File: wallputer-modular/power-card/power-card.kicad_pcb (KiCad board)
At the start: 2 copper layers, 142 parts, among them J2 Power, Q1 FQP27P06, Q2 IRLZ44N, SW1 reset, U1 TLC555CD, U12 74HC04, U16 74HC04, U17 74HC04, U18 74HC04, U2 74HC04, U3 74HC04

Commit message: fix drc
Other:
- board outline added: 100.3 x 99.7 mm

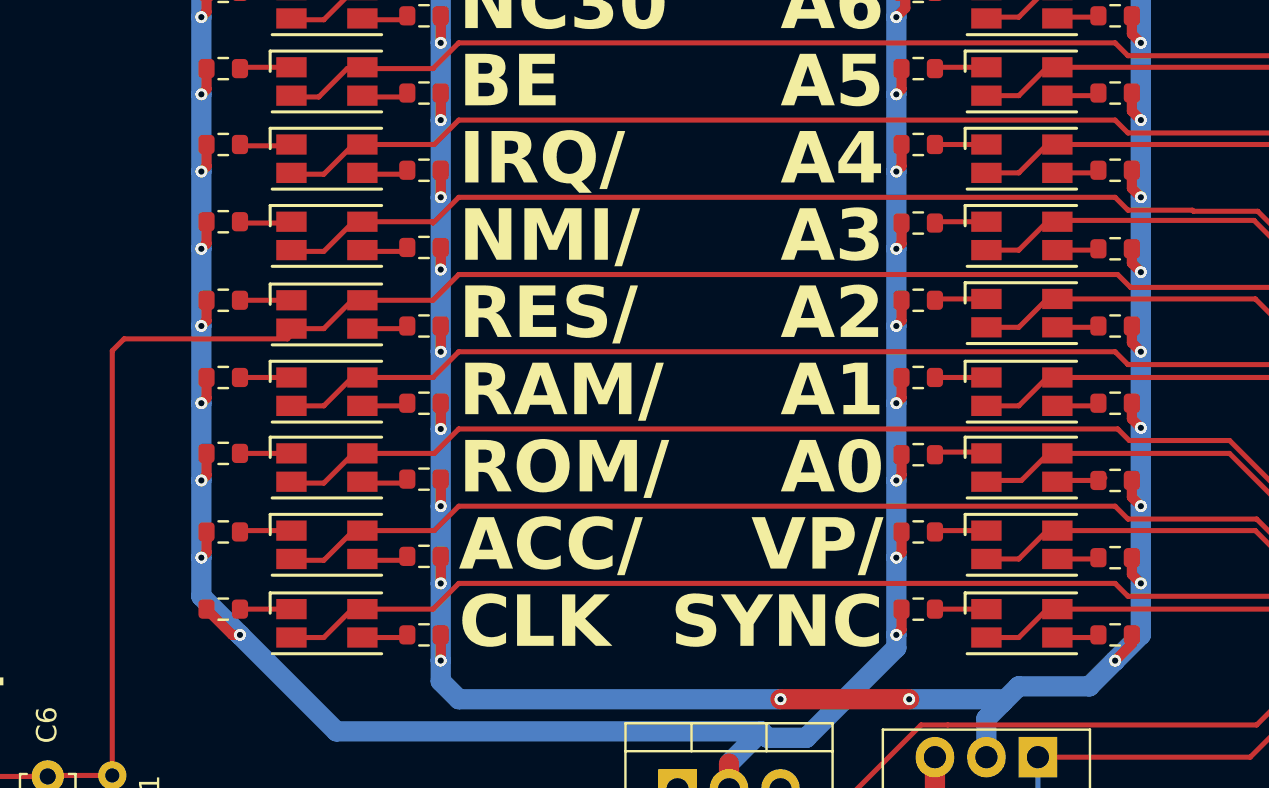
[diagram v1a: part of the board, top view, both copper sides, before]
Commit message: replace dual leds with single for some signals
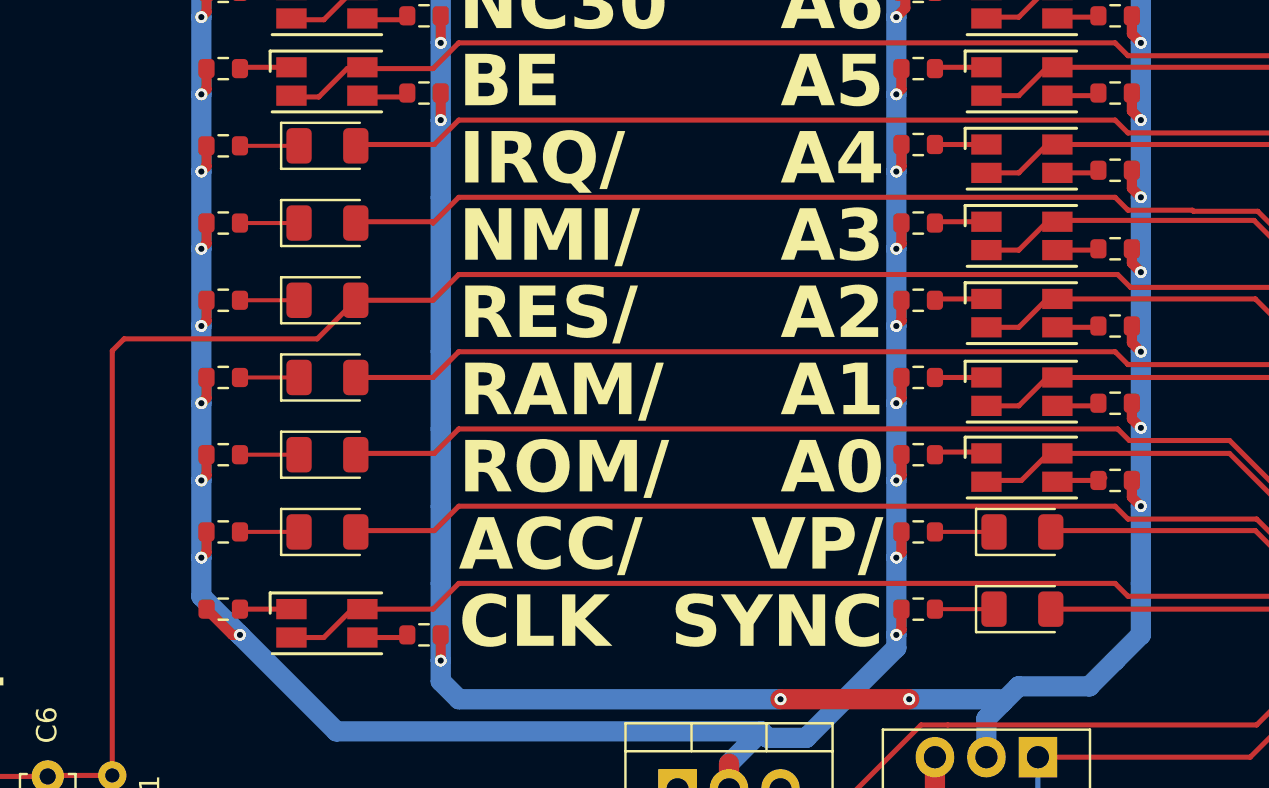
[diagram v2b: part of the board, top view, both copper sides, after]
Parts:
- removed R21, R22, R43, R44, R72, R73, R79, R80: 680, Resistor_SMD:R_0603_1608Metric
- D12, D19, D20, D37, D4, D6, D7, D8: value Wallputer_Dual_LED -> blue; footprint Wallputer:Wallputer_Dual_LED -> LED_SMD:LED_1206_3216Metric
- R10, R11, R12, R5, R6, R7, R8, R9: value 680 -> 1k
- moved R12 37.5 mm to (86.2, 116.8)
- moved R9 24.5 mm to (120.5, 132.1), turned to 0 degrees
- moved R6 16.1 mm to (86.2, 109.2), turned to 0 degrees
- moved R8 11.4 mm to (86.2, 113.0)
- moved R11 11.0 mm to (120.5, 128.3), turned to 0 degrees
- moved R7 9.98 mm to (86.2, 124.5), turned to 0 degrees
- moved D37 0.70 mm to (91.3, 116.8)
- moved D4 0.70 mm to (91.3, 120.7)
- moved D8 0.70 mm to (125.6, 132.1)
- moved D19 0.64 mm to (91.3, 109.2)
- moved D20 0.64 mm to (91.3, 113.0)
- moved D6 0.64 mm to (91.3, 124.5)
- moved D7 0.64 mm to (91.3, 128.3)
- moved D12 0.64 mm to (125.6, 128.3)
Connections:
- D12 pad 1: Net-(D12-Green_A) -> Net-(D12-K)
- D12 pad 2: Net-(D12-Red_A) -> Net-(D12-A)
- D19 pad 1: Net-(D19-Green_A) -> Net-(D19-K)
- D19 pad 2: Net-(D19-Red_A) -> Net-(D19-A)
- D20 pad 1: Net-(D20-Green_A) -> Net-(D20-K)
- D20 pad 2: Net-(D20-Red_A) -> Net-(D20-A)
- D37 pad 1: RES/ -> Net-(D37-K)
- D37 pad 2: Net-(D37-Red_A) -> RES/
- D4 pad 1: Net-(D4-Green_A) -> Net-(D4-K)
- D4 pad 2: Net-(D4-Red_A) -> Net-(D4-A)
- D6 pad 1: Net-(D6-Green_A) -> Net-(D6-K)
- D6 pad 2: Net-(D6-Red_A) -> Net-(D6-A)
- D7 pad 1: Net-(D7-Green_A) -> Net-(D7-K)
- D7 pad 2: Net-(D7-Red_A) -> Net-(D7-A)
- D8 pad 1: Net-(D8-Green_A) -> Net-(D8-K)
- D8 pad 2: Net-(D8-Red_A) -> Net-(D8-A)
- R10 pad 2: Net-(D7-Red_A) -> Net-(D7-K)
- R11 pad 1: Net-(Q1-D) -> Net-(Q2-D)
- R11 pad 2: Net-(D8-Green_K) -> Net-(D12-K)
- R12 pad 2: Net-(D8-Red_A) -> Net-(D37-K)
- R5 pad 2: Net-(D4-Red_A) -> Net-(D4-K)
- R6 pad 1: Net-(Q1-D) -> Net-(Q2-D)
- R6 pad 2: Net-(D4-Green_K) -> Net-(D19-K)
- R7 pad 1: Net-(Q1-D) -> Net-(Q2-D)
- R7 pad 2: Net-(D6-Green_K) -> Net-(D6-K)
- R8 pad 2: Net-(D6-Red_A) -> Net-(D20-K)
- R9 pad 1: Net-(Q1-D) -> Net-(Q2-D)
- R9 pad 2: Net-(D7-Green_K) -> Net-(D8-K)
- U12 pad 12: Net-(D4-Green_A) -> Net-(D4-A)
- U12 pad 8: Net-(D20-Green_A) -> Net-(D20-A)
- U2 pad 12: Net-(D19-Green_A) -> Net-(D19-A)
- U3 pad 10: Net-(D7-Green_A) -> Net-(D7-A)
- U3 pad 2: Net-(D8-Green_A) -> Net-(D8-A)
- U3 pad 4: Net-(D12-Green_A) -> Net-(D12-A)
- U3 pad 8: Net-(D6-Green_A) -> Net-(D6-A)
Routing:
- net Net-(D6-Green_A): track 59.9 -> 0.00 mm
- net Net-(D7-Green_A): track 59.3 -> 0.00 mm
- net Net-(D20-Green_A): track 59.3 -> 0.00 mm
- net Net-(D4-Green_A): track 58.2 -> 0.00 mm
- net Net-(D19-Green_A): track 57.6 -> 0.00 mm
- net Net-(D6-A): track 0.00 -> 55.8 mm
- net Net-(D7-A): track 0.00 -> 55.3 mm
- net Net-(D20-A): track 0.00 -> 55.2 mm
- net Net-(D4-A): track 0.00 -> 54.6 mm
- net Net-(D19-A): track 0.00 -> 53.6 mm
- net Net-(D12-Green_A): track 29.5 -> 0.00 mm
- net Net-(D8-Green_A): track 29.0 -> 0.00 mm
- net Net-(D12-A): track 0.00 -> 26.0 mm
- net Net-(D8-A): track 0.00 -> 25.4 mm
- net Net-(Q1-D): track 219.0 -> 208.6 mm, vias 38 -> 30
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
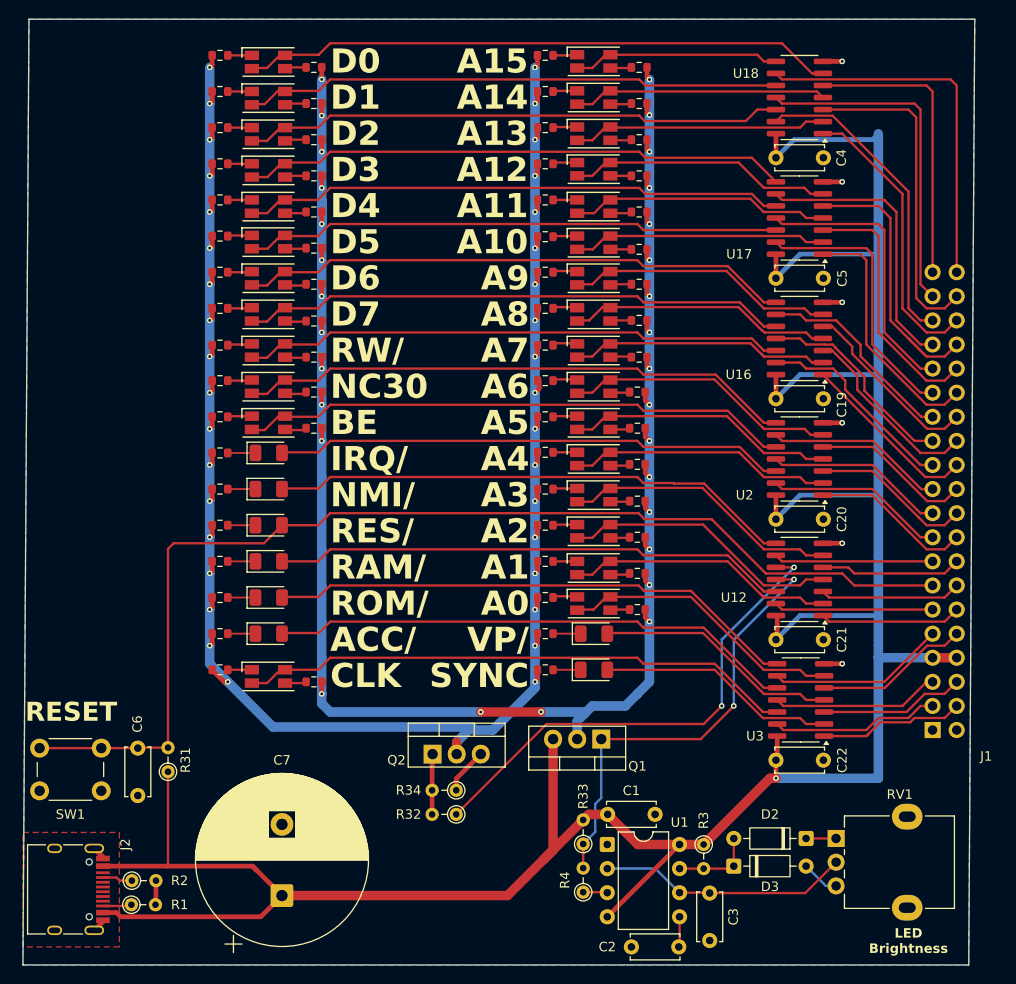
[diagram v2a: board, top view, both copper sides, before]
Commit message: shift connector up
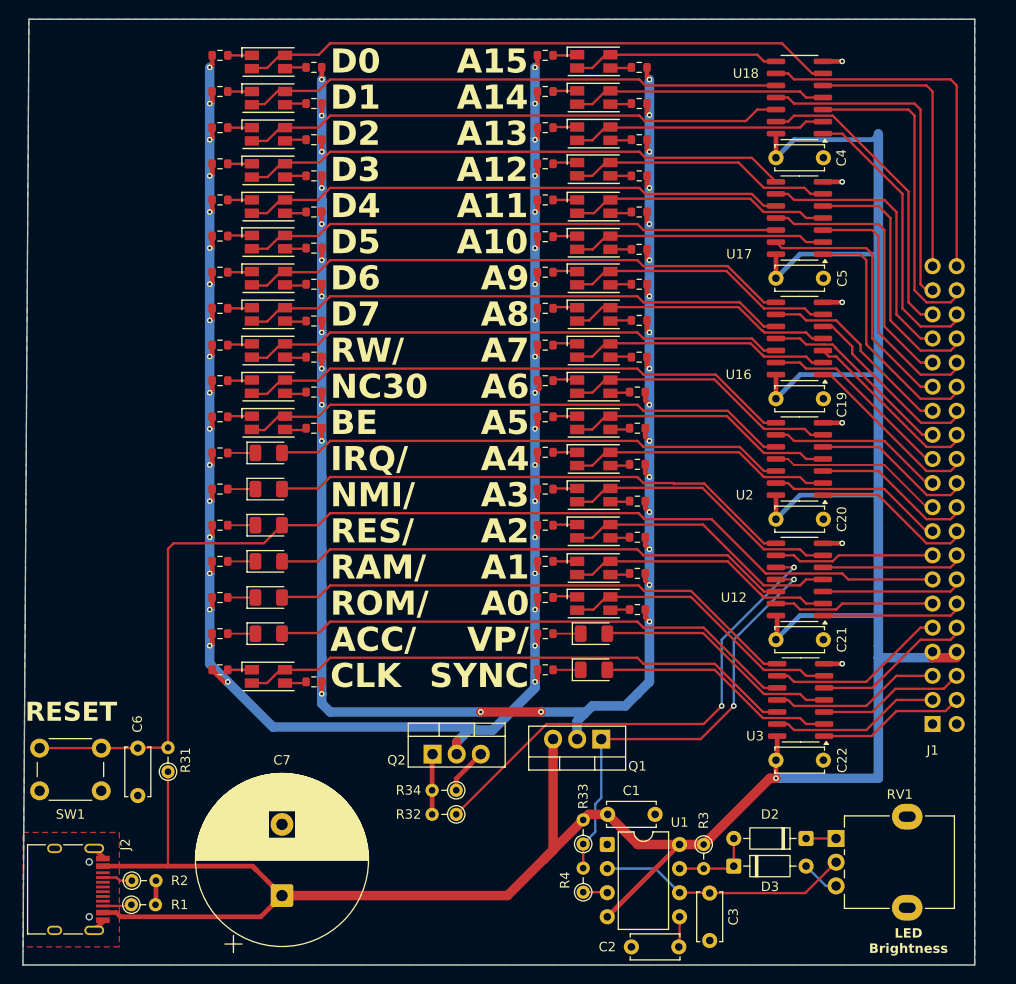
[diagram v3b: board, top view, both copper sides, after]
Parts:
- moved J1 0.64 mm to (161.3, 137.8)
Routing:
- net A12: track 30.1 -> 27.0 mm
- net A8: track 20.0 -> 18.6 mm
- net D7: track 21.9 -> 20.7 mm
- net A14: track 34.5 -> 33.6 mm
- net RW/: track 21.5 -> 20.7 mm
- net D5: track 28.7 -> 28.0 mm
- net D3: track 29.8 -> 29.1 mm
- net D2: track 32.9 -> 32.3 mm
- net D4: track 29.4 -> 28.8 mm
- net D6: track 21.7 -> 21.1 mm
- net A5: track 17.0 -> 16.5 mm
- net A3: track 14.9 -> 14.4 mm
- net A10: track 26.4 -> 25.9 mm
- net A9: track 19.6 -> 19.0 mm
- net A1: track 14.9 -> 14.4 mm
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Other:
- outline, holes or cut-outs redrawn

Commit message: fine-tuning
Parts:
- moved R31 1.98 mm to (82.7, 142.8)
- moved SW1 1.98 mm to (69.1, 140.3)
- moved C6 1.98 mm to (79.5, 140.3)
- moved R1 0.70 mm to (77.5, 156.8)
- moved J2 0.69 mm to (70.5, 155.2)
- moved R2 0.69 mm to (77.6, 154.3)
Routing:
- net RES/: track 119.2 -> 116.9 mm
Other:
- board size 100.3 x 99.7 mm -> 99.7 x 99.7 mm
